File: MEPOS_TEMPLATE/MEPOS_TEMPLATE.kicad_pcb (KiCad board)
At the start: 4 copper layers, 101.6 x 101.6 mm, 10 parts, among them J201 Conn_02x32_Odd_Even, J202 Conn_02x20_Odd_Even

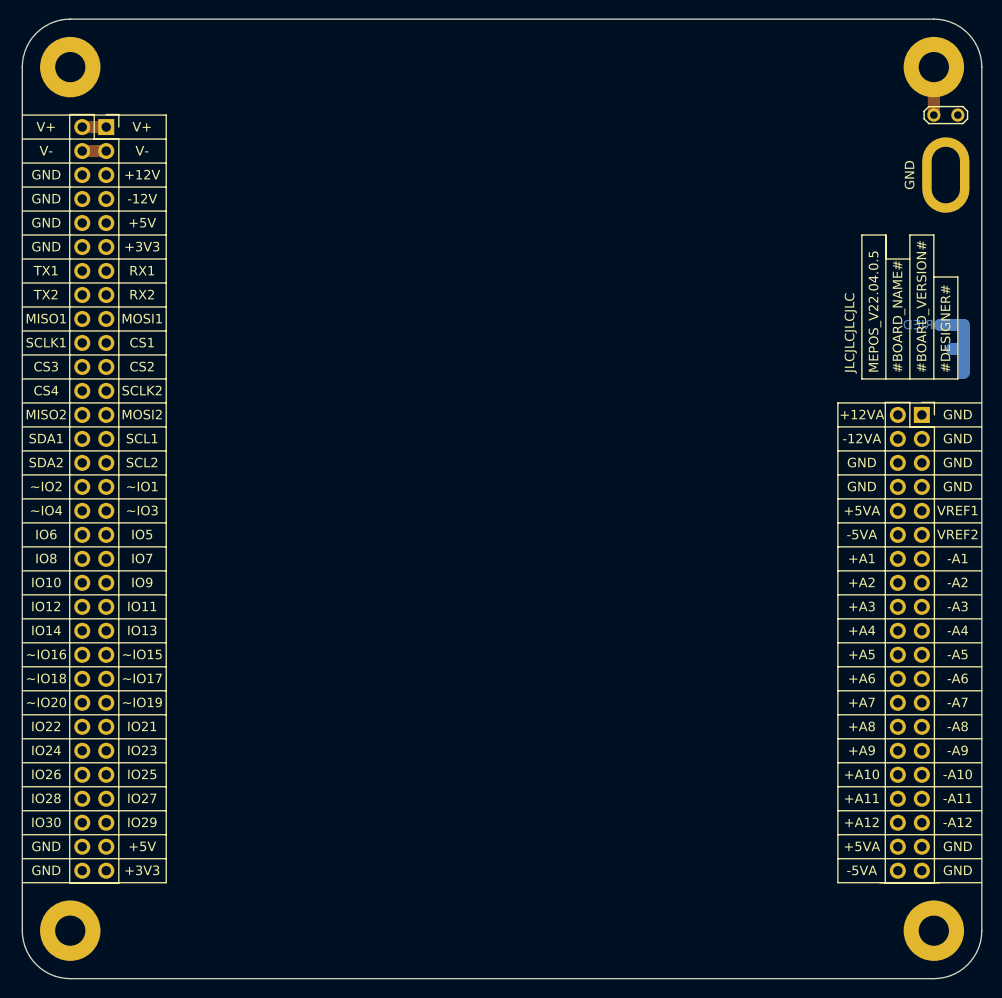
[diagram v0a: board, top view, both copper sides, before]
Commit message: Updated to MEPOS V22.07.0.51
Added fiducial markers to the topside of the board
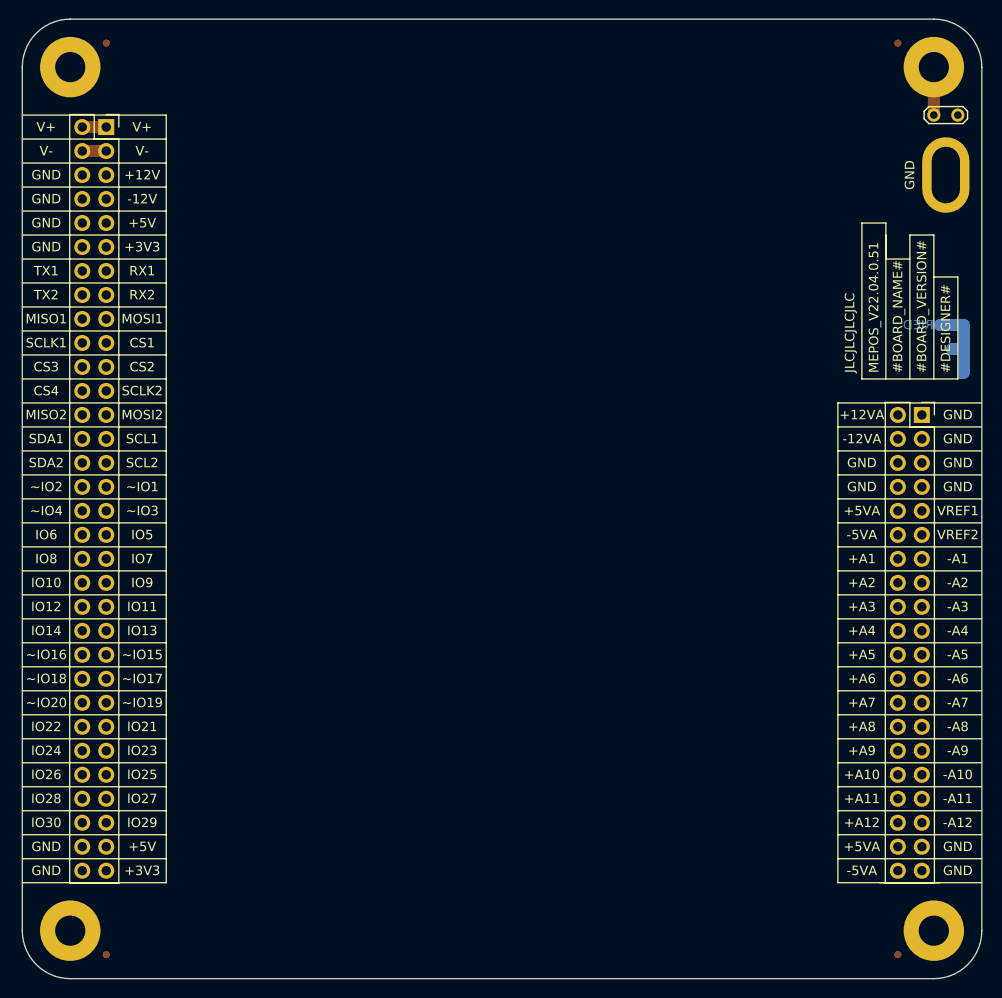
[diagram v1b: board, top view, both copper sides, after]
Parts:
- added FID1: Fiducial, Fiducial:Fiducial_0.75mm_Mask1.5mm, F.Cu at (103.0, 36.5)
- added FID2: Fiducial, Fiducial:Fiducial_0.75mm_Mask1.5mm, F.Cu at (103.0, 133.0)
- added FID3: Fiducial, Fiducial:Fiducial_0.75mm_Mask1.5mm, F.Cu at (186.8, 133.0)
- added FID4: Fiducial, Fiducial:Fiducial_0.75mm_Mask1.5mm, F.Cu at (186.8, 36.5)
- GND1: renamed from GND201; footprint MEP_TEMPLATE:Scope_GND -> MEPOS:Scope_GND
- renumbered H201 to H1, H202 to H2, H203 to H3, H204 to H4, J201 to J1, J202 to J2, JP201 to JP1
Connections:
- net GPIO1 renamed GPIO1~
- net GPIO15 renamed GPIO15~
- net GPIO16 renamed GPIO16~
- net GPIO17 renamed GPIO17~
- net GPIO18 renamed GPIO18~
- net GPIO19 renamed GPIO19~
- net GPIO2 renamed GPIO2~
- net GPIO20 renamed GPIO20~
- net GPIO3 renamed GPIO3~
- net GPIO4 renamed GPIO4~
- J2 pad 37: GNDA -> GND
- J2 pad 39: GNDA -> GND
- J2 pad 5: GNDA -> GND
- J2 pad 6: +3V3A -> GND
- J2 pad 7: GNDA -> GND
- J2 pad 8: -3V3A -> GND
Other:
- board text added: "MEPOS_V22.04.0.51"
- board text removed: "MEPOS_V22.04.0.5"
